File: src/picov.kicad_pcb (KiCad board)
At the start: 2 copper layers, 21.2 x 51.3 mm, 42 parts, among them J1 USB_C_Receptacle_USB2.0_16P, J2 Conn_01x20, J3 Conn_01x20, J4 Conn_01x03, J5 Conn_01x06, SW1 SW_Push, SW2 SW_Push, SW3 SW_Push, U1 RP2040, U10 WS2812-2020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

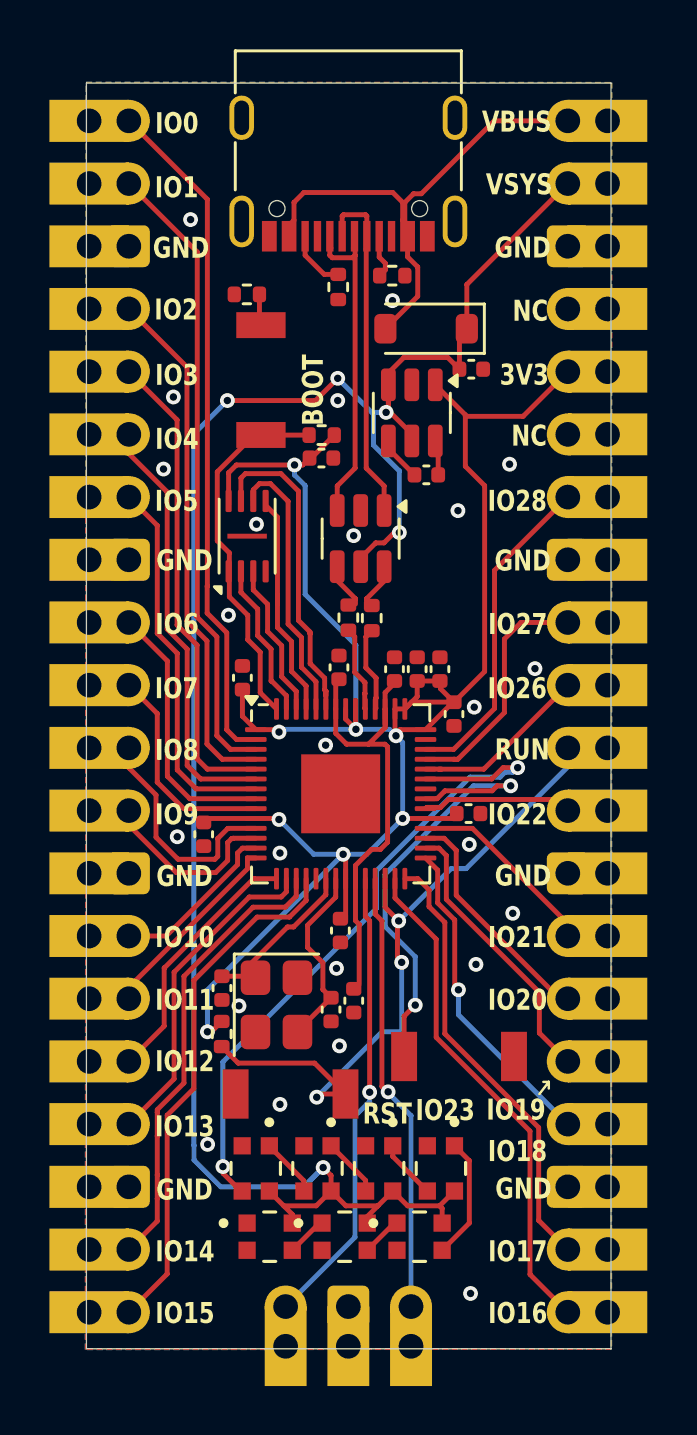
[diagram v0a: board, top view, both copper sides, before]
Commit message: removed castellated holes due to high jlcpcb pricing, finished 4x4 neopixel matrix
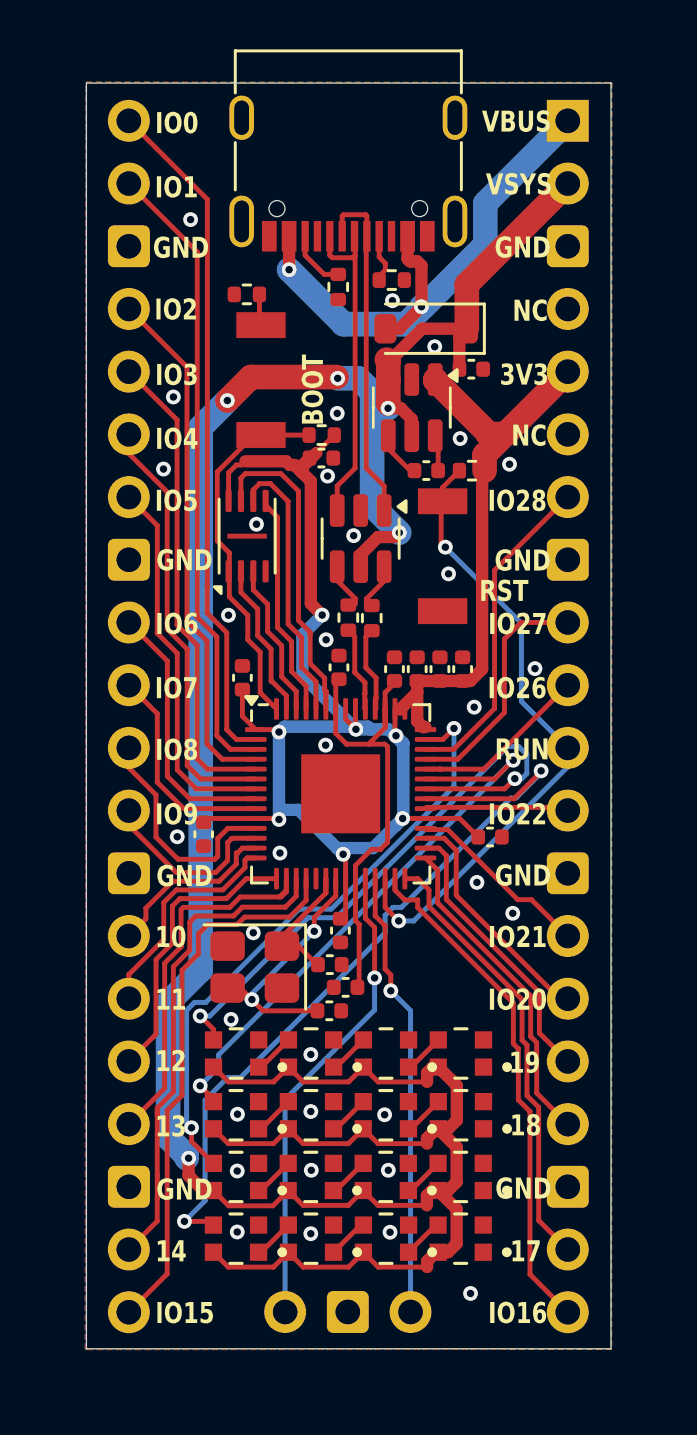
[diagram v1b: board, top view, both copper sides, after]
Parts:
- removed SW3: SW_Push, Button_Switch_SMD:SMD_3x4
- added U12: WS2812-2020, WS2812-2020:LED_WS2812-2020, F.Cu at (181.6, 87.8)
- added U13: WS2812-2020, WS2812-2020:LED_WS2812-2020, F.Cu at (181.6, 90.3)
- added U14: WS2812-2020, WS2812-2020:LED_WS2812-2020, F.Cu at (184.6, 87.8)
- added U15: WS2812-2020, WS2812-2020:LED_WS2812-2020, F.Cu at (184.6, 90.3)
- added U16: WS2812-2020, WS2812-2020:LED_WS2812-2020, F.Cu at (187.6, 87.8)
- added U17: WS2812-2020, WS2812-2020:LED_WS2812-2020, F.Cu at (187.6, 90.3)
- added U18: WS2812-2020, WS2812-2020:LED_WS2812-2020, F.Cu at (190.7, 87.8)
- added U19: WS2812-2020, WS2812-2020:LED_WS2812-2020, F.Cu at (190.7, 90.3)
- added U2: WS2812-2020, WS2812-2020:LED_WS2812-2020, F.Cu at (181.6, 82.8)
- J2, J3: footprint Connector_PinHeader_2.54mm:Castellated_20 -> Connector_PinHeader_2.54mm:PinHeader_1x20_P2.54mm_Vertical
- J4: moved to B.Cu
- moved R7 25.0 mm to (191.1, 59.2), turned to 180 degrees
- moved SW2 22.6 mm to (189.9, 62.6), turned to -90 degrees
- moved U11 10.7 mm to (190.7, 82.8), turned to 0 degrees
- moved U9 8.62 mm to (184.6, 82.8), turned to 0 degrees
- moved U10 7.61 mm to (187.6, 82.8), turned to 0 degrees
- moved C15 4.47 mm to (185.4, 79.2), turned to 180 degrees
- moved U8 2.30 mm to (190.7, 85.3), turned to 0 degrees
- moved U5 2.30 mm to (181.6, 85.3), turned to 0 degrees
- moved U7 2.17 mm to (187.6, 85.3), turned to 0 degrees
- moved U6 2.17 mm to (184.6, 85.3), turned to 0 degrees
- moved C3 1.85 mm to (190.7, 67.2), turned to -90 degrees
- moved Y1 1.77 mm to (182.3, 79.3), turned to 180 degrees
- moved C4 1.29 mm to (191.8, 74.0)
- moved C13 0.63 mm to (186.0, 80.1), turned to 180 degrees
- moved J4 0.22 mm to (183.6, 93.2), turned to -90 degrees
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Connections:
- U8 pad 1: Net-(U8-DO) -> unconnected-(U8-DO-Pad1)
- U9 pad 3: Net-(U8-DO) -> Net-(U2-DO)
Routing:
- net VSYS: track 82.5 -> 119.4 mm
- net IO29: track 0.00 -> 24.8 mm, vias 0 -> 2
- net IO24: track 0.00 -> 24.2 mm, vias 0 -> 2
- net IO23: track 18.3 -> 31.3 mm
- net Net-(U8-DO): track 4.93 -> 0.00 mm
- net IO25: track 27.3 -> 23.2 mm
- net +5V: track 20.8 -> 24.4 mm, vias 0 -> 2
- net RUN: track 28.3 -> 25.4 mm, vias 3 -> 2
- net XOUT: track 7.64 -> 10.3 mm, vias 0 -> 2
- net IO13: track 13.3 -> 15.4 mm
- net Net-(U15-DO): track 0.00 -> 1.67 mm
- net Net-(U2-DO): track 0.00 -> 1.66 mm
- net Net-(U16-DO): track 0.00 -> 1.66 mm
- net Net-(U14-DO): track 0.00 -> 1.66 mm
- net Net-(U13-DO): track 0.00 -> 1.66 mm
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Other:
- board text added: "10"
- board text added: "11"
- board text added: "12"
- board text added: "13"
- board text added: "14"
- board text added: "17"
- board text added: "18"
- board text added: "19"
- board text removed: "IO10"
- board text removed: "IO11"
- board text removed: "IO12"
- board text removed: "IO13"
- board text removed: "IO14"
- board text removed: "IO17"
- board text removed: "IO18"
- board text removed: "IO19"
- board text removed: "IO23"

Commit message: changed some routing
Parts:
- moved C15 5.60 mm to (179.9, 80.6), turned to -90 degrees
- moved C1 2.35 mm to (186.5, 80.0), turned to 180 degrees
- moved C16 2.18 mm to (185.1, 78.9), turned to 90 degrees
- moved C13 1.54 mm to (186.6, 78.7), turned to -90 degrees
- moved Y1 0.50 mm to (182.5, 79.7), turned to 0 degrees
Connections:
- R1 pad 1: CLEAN_USBDP -> USBDP
- R2 pad 2: CLEAN_USBDN -> USBDN
- U4 pad 4: CLEAN_USBDP -> USBDP
- U4 pad 6: CLEAN_USBDN -> USBDN
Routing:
- net IO23: track 31.3 -> 36.7 mm
- net USBDN: track 13.6 -> 18.4 mm
- net XOUT: track 10.3 -> 5.67 mm, vias 2 -> 0
- net USBDP: track 13.0 -> 17.6 mm
- net XIN: track 5.85 -> 9.33 mm
- net IO25: track 23.2 -> 26.0 mm
- net +3V3: track 83.1 -> 85.7 mm
- net +1V1: track 18.7 -> 16.9 mm
- net IO29: track 24.8 -> 26.5 mm
- net CLEAN_USBDP: track 1.60 -> 0.00 mm
- net CLEAN_USBDN: track 1.60 -> 0.00 mm
- net IO24: track 24.2 -> 25.6 mm
- net SWCLK: track 19.2 -> 19.9 mm
- net GND: vias 34 -> 37
